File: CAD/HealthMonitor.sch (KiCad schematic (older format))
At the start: 8 parts

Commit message: Created sheet hierarchy"
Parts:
- removed C1: 1u, symbol Device:C
- removed D1, D2: LED_green, symbol Device:LED
- removed D3: LED_ir, symbol Device:LED
- removed R1, R2, R3: 10k, symbol Device:R
- removed U?: BH1792GLC, symbol bh1792glc:BH1792GLC
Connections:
- net labels removed: GND, VCC
- wire segments 33 -> 0
- no-connect marks 1 -> 0
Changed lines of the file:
@@
 EESchema Schematic File Version 4
+LIBS:HealthMonitor-cache
 EELAYER 26 0
 EELAYER END
 $Descr A4 11693 8268
 encoding utf-8
-Sheet 1 1
+Sheet 1 2
 Title ""
 Date ""
@@
 Comment4 ""
 $EndDescr
-$Comp
-L bh1792glc:BH1792GLC U?
-U 1 1 5CC0C673
-P 6050 3400
-F 0 "U?" H 6025 3865 50  0000 C CNN
-F 1 "BH1792GLC" H 6025 3774 50  0000 C CNN
-F 2 "" H 6050 3400 50  0001 C CNN
-F 3 "" H 6050 3400 50  0001 C CNN
-	1    6050 3400
-	1    0    0    -1
-$EndComp
-$Comp
-L Device:LED D3
-U 1 1 5CC0C7AE
-P 4500 2950
-F 0 "D3" V 4550 3250 50  0000 R CNN
-F 1 "LED_ir" V 4450 3300 50  0000 R CNN
-F 2 "" H 4500 2950 50  0001 C CNN
-F 3 "~" H 4500 2950 50  0001 C CNN
-	1    4500 2950
-	0    -1   -1   0
-$EndComp
-Wire Wire Line
-	5500 3400 5000 3400
-Wire Wire Line
-	5000 3400 5000 3100
-Wire Wire Line
-	4750 3500 4750 3100
-Wire Wire Line
-	4750 3500 5500 3500
-Wire Wire Line
-	4500 3600 5500 3600
-$Comp
-L Device:LED D2
-U 1 1 5CC0C8EA
-P 4750 2950
-F 0 "D2" V 4800 2850 50  0000 R CNN
-F 1 "LED_green" V 4900 3100 50  0000 R CNN
-F 2 "" H 4750 2950 50  0001 C CNN
-F 3 "~" H 4750 2950 50  0001 C CNN
-	1    4750 2950
-	0    -1   -1   0
-$EndComp
-$Comp
-L Device:LED D1
-U 1 1 5CC0C908
-P 5000 2950
-F 0 "D1" V 5038 2832 50  0000 R CNN
-F 1 "LED_green" V 4950 2850 50  0000 R CNN
-F 2 "" H 5000 2950 50  0001 C CNN
-F 3 "~" H 5000 2950 50  0001 C CNN
-	1    5000 2950
-	0    -1   -1   0
-$EndComp
-Wire Wire Line
-	4500 3100 4500 3600
-Wire Wire Line
-	4500 2800 4500 2600
-Wire Wire Line
-	4500 2600 4750 2600
-Wire Wire Line
-	5000 2600 5000 2800
-Wire Wire Line
-	4750 2800 4750 2600
-Connection ~ 4750 2600
-Wire Wire Line
-	5500 3200 5500 2600
-Wire Wire Line
-	5500 2600 5400 2600
-Connection ~ 5000 2600
-$Comp
-L power:GND #PWR?
-U 1 1 5CC0CC3B
-P 5350 3300
-F 0 "#PWR?" H 5350 3050 50  0001 C CNN
-F 1 "GND" V 5355 3172 50  0000 R CNN
-F 2 "" H 5350 3300 50  0001 C CNN
-F 3 "" H 5350 3300 50  0001 C CNN
-	1    5350 3300
-	0    1    1    0
-$EndComp
-Wire Wire Line
-	5350 3300 5400 3300
-$Comp
-L power:VCC #PWR?
-U 1 1 5CC0CDAD
-P 5050 2500
-F 0 "#PWR?" H 5050 2350 50  0001 C CNN
-F 1 "VCC" H 5067 2673 50  0000 C CNN
-F 2 "" H 5050 2500 50  0001 C CNN
-F 3 "" H 5050 2500 50  0001 C CNN
-	1    5050 2500
-	1    0    0    -1
-$EndComp
-Wire Wire Line
-	5050 2500 5050 2600
-Connection ~ 5050 2600
-Wire Wire Line
-	5050 2600 5000 2600
-Wire Wire Line
-	4750 2600 5000 2600
-$Comp
-L Device:C C1
-U 1 1 5CC0D0E2
-P 5400 2900
-F 0 "C1" H 5515 2946 50  0000 L CNN
-F 1 "1u" H 5515 2855 50  0000 L CNN
-F 2 "" H 5438 2750 50  0001 C CNN
-F 3 "~" H 5400 2900 50  0001 C CNN
-	1    5400 2900
-	1    0    0    -1
-$EndComp
-Connection ~ 5400 3300
-Wire Wire Line
-	5400 3300 5500 3300
-Connection ~ 5400 2600
-Wire Wire Line
-	5400 2600 5050 2600
-Wire Wire Line
-	5400 2750 5400 2600
-Wire Wire Line
-	5400 3050 5400 3300
-$Comp
-L Device:R R1
-U 1 1 5CC0D78E
-P 6700 2850
-F 0 "R1" H 6770 2896 50  0000 L CNN
-F 1 "10k" H 6770 2805 50  0000 L CNN
-F 2 "" V 6630 2850 50  0001 C CNN
-F 3 "~" H 6700 2850 50  0001 C CNN
-	1    6700 2850
-	1    0    0    -1
-$EndComp
-$Comp
-L Device:R R2
-U 1 1 5CC0D826
-P 6950 2850
-F 0 "R2" H 7020 2896 50  0000 L CNN
-F 1 "10k" H 7020 2805 50  0000 L CNN
-F 2 "" V 6880 2850 50  0001 C CNN
-F 3 "~" H 6950 2850 50  0001 C CNN
-	1    6950 2850
-	1    0    0    -1
-$EndComp
-$Comp
-L Device:R R3
-U 1 1 5CC0D850
-P 7200 2850
-F 0 "R3" H 7270 2896 50  0000 L CNN
-F 1 "10k" H 7270 2805 50  0000 L CNN
-F 2 "" V 7130 2850 50  0001 C CNN
-F 3 "~" H 7200 2850 50  0001 C CNN
-	1    7200 2850
-	1    0    0    -1
-$EndComp
-Wire Wire Line
-	7200 2700 7200 2600
-Wire Wire Line
-	7200 2600 6950 2600
-Connection ~ 5500 2600
-Wire Wire Line
-	6700 2700 6700 2600
-Connection ~ 6700 2600
-Wire Wire Line
-	6700 2600 5500 2600
-Wire Wire Line
-	6950 2700 6950 2600
-Connection ~ 6950 2600
-Wire Wire Line
-	6950 2600 6700 2600
-Wire Wire Line
-	6700 3000 6700 3200
-Wire Wire Line
-	6700 3200 6550 3200
-Wire Wire Line
-	6550 3300 6950 3300
-Wire Wire Line
-	6950 3300 6950 3000
-Wire Wire Line
-	6550 3600 7200 3600
-Wire Wire Line
-	7200 3600 7200 3000
-$Comp
-L power:GND #PWR?
-U 1 1 5CC0E6E1
-P 6700 3500
-F 0 "#PWR?" H 6700 3250 50  0001 C CNN
-F 1 "GND" V 6705 3372 50  0000 R CNN
-F 2 "" H 6700 3500 50  0001 C CNN
-F 3 "" H 6700 3500 50  0001 C CNN
-	1    6700 3500
-	0    -1   -1   0
-$EndComp
-Wire Wire Line
-	6550 3500 6700 3500
-NoConn ~ 6550 3400
+$Sheet
+S 8050 2800 1600 2300
+U 5CD03BDA
+F0 "bh1792-interface" 50
+F1 "bh1792-interface.sch" 50
+$EndSheet
 $EndSCHEMATC

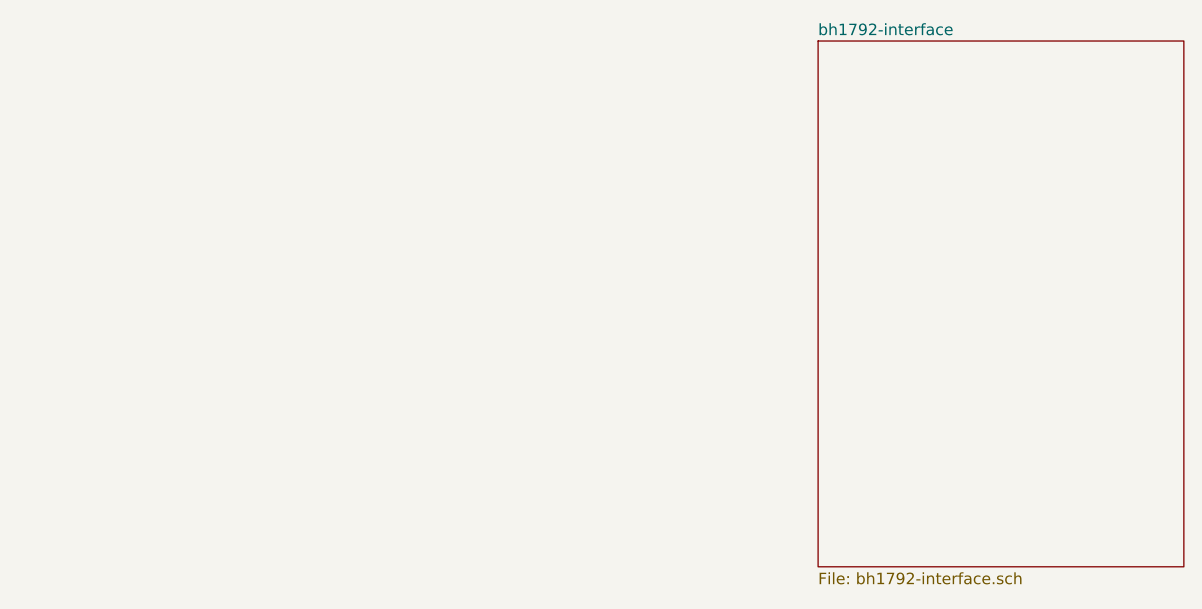
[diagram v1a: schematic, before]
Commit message: Created Power PCB, both schematic and layout
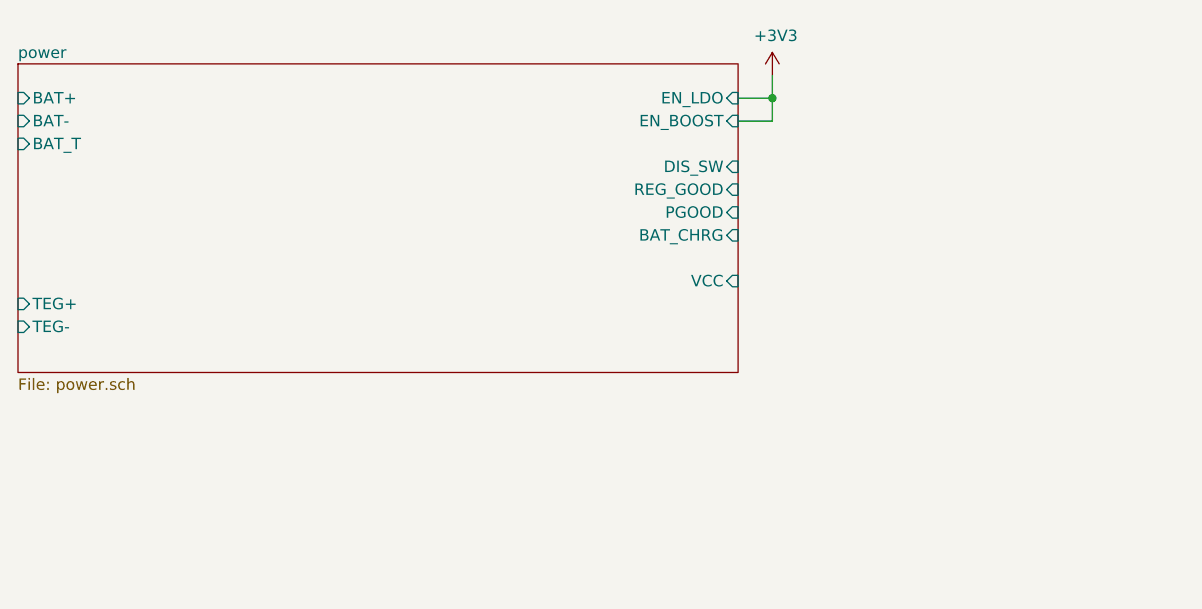
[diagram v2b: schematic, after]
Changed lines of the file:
@@
 $EndDescr
 $Sheet
-S 8050 2800 1600 2300
-U 5CD03BDA
-F0 "bh1792-interface" 50
-F1 "bh1792-interface.sch" 50
+S 4550 2900 3150 1350
+U 5CD0623C
+F0 "power" 50
+F1 "power.sch" 50
+F2 "BAT+" I L 4550 3050 50
+F3 "EN_LDO" I R 7700 3050 50
+F4 "EN_BOOST" I R 7700 3150 50
+F5 "DIS_SW" I R 7700 3350 50
+F6 "REG_GOOD" I R 7700 3450 50
+F7 "PGOOD" I R 7700 3550 50
+F8 "BAT-" I L 4550 3150 50
+F9 "TEG+" I L 4550 3950 50
+F10 "TEG-" I L 4550 4050 50
+F11 "BAT_T" I L 4550 3250 50
+F12 "BAT_CHRG" I R 7700 3650 50
+F13 "VCC" I R 7700 3850 50
 $EndSheet
+Wire Wire Line
+	7700 3150 7850 3150
+Wire Wire Line
+	7850 3050 7700 3050
+Wire Wire Line
+	7850 3050 7850 3150
+$Comp
+L power:+3V3 #PWR0101
+U 1 1 5CD4D077
+P 7850 2950
+F 0 "#PWR0101" H 7850 2800 50  0001 C CNN
+F 1 "+3V3" H 7865 3123 50  0000 C CNN
+F 2 "" H 7850 2950 50  0001 C CNN
+F 3 "" H 7850 2950 50  0001 C CNN
+	1    7850 2950
+	1    0    0    -1
+$EndComp
+Wire Wire Line
+	7850 2950 7850 3050
+Connection ~ 7850 3050
 $EndSCHEMATC

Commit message: Finished PCB Draft -- waiting for review
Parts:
- added J1: BAT_T, Connector_PinHeader_1.27mm:PinHeader_1x01_P1.27mm_Vertical, symbol Connector:Conn_01x01_Male
- added J10, J20: SDA, Connector_PinHeader_1.27mm:PinHeader_1x01_P1.27mm_Vertical, symbol Connector:Conn_01x01_Male
- added J11, J21: SCL, Connector_PinHeader_1.27mm:PinHeader_1x01_P1.27mm_Vertical, symbol Connector:Conn_01x01_Male
- added J12, J25: DIS_SW, Connector_PinHeader_1.27mm:PinHeader_1x01_P1.27mm_Vertical, symbol Connector:Conn_01x01_Male
- added J13, J24: BAT_CHRG, Connector_PinHeader_1.27mm:PinHeader_1x01_P1.27mm_Vertical, symbol Connector:Conn_01x01_Male
- added J14: USBDP, Connector_PinHeader_1.27mm:PinHeader_1x01_P1.27mm_Vertical, symbol Connector:Conn_01x01_Male
- added J15: USBDM, Connector_PinHeader_1.27mm:PinHeader_1x01_P1.27mm_Vertical, symbol Connector:Conn_01x01_Male
- added J16: USB_V, Connector_PinHeader_1.27mm:PinHeader_1x01_P1.27mm_Vertical, symbol Connector:Conn_01x01_Male
- added J17: VBUS, Connector_PinHeader_1.27mm:PinHeader_1x01_P1.27mm_Vertical, symbol Connector:Conn_01x01_Male
- added J18: D+, Connector_PinHeader_1.27mm:PinHeader_1x01_P1.27mm_Vertical, symbol Connector:Conn_01x01_Male
- added J19: D-, Connector_PinHeader_1.27mm:PinHeader_1x01_P1.27mm_Vertical, symbol Connector:Conn_01x01_Male
- added J2: TEG+, Connector_PinHeader_1.27mm:PinHeader_1x01_P1.27mm_Vertical, symbol Connector:Conn_01x01_Male
- added J22, J8: VCC, Connector_PinHeader_1.27mm:PinHeader_1x01_P1.27mm_Vertical, symbol Connector:Conn_01x01_Male
- added J23, J9: GND, Connector_PinHeader_1.27mm:PinHeader_1x01_P1.27mm_Vertical, symbol Connector:Conn_01x01_Male
- added J3: TEG-, Connector_PinHeader_1.27mm:PinHeader_1x01_P1.27mm_Vertical, symbol Connector:Conn_01x01_Male
- added J4: BAT-, Connector_PinHeader_1.27mm:PinHeader_1x01_P1.27mm_Vertical, symbol Connector:Conn_01x01_Male
- added J5: BAT+, Connector_PinHeader_1.27mm:PinHeader_1x01_P1.27mm_Vertical, symbol Connector:Conn_01x01_Male
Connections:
- net +3V3: now also J22.1 (Pin_1), J8.1 (Pin_1)
- net power/BAT+: now also J5.1 (Pin_1)
- net power/BAT_T: now also J1.1 (Pin_1)
- net power/TEG+: now also J2.1 (Pin_1)
- new net BAT_CHRG: J13.1 (Pin_1), J24.1 (Pin_1)
- new net DIS_SW: J12.1 (Pin_1), J25.1 (Pin_1)
- new net GND: J23.1 (Pin_1), J3.1 (Pin_1), J4.1 (Pin_1), J9.1 (Pin_1)
- new net SCL: J11.1 (Pin_1), J21.1 (Pin_1)
- new net SDA: J10.1 (Pin_1), J20.1 (Pin_1)
- new net power/USBD+: J14.1 (Pin_1), J18.1 (Pin_1)
- new net power/USBD-: J15.1 (Pin_1), J19.1 (Pin_1)
- new net power/USB_VBUS: J16.1 (Pin_1), J17.1 (Pin_1)

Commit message: rescue commit
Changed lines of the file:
@@
-$EndSheet
-$Sheet
-S 8750 950  1350 2000
-U 5CD82074
-F0 "IMUSensor" 50
-F1 "IMUSensor.sch" 50
-F2 "VDD" I L 8750 1150 50
-F3 "SCL" I L 8750 1450 50
-F4 "SDA-SDISDO" B L 8750 1550 50
-F5 "SDO-SA0" B L 8750 1650 50
-F6 "CS" I L 8750 1750 50
-F7 "INT2" O L 8750 2000 50
-F8 "INT1" O L 8750 2100 50
-F9 "GND" U L 8750 1250 50
 $EndSheet
 $Sheet
@@
 Wire Wire Line
 	8200 3550 8900 3550
+$Sheet
+S 8750 950  1350 2000
+U 5CD82074
+F0 "IMUSensor" 50
+F1 "IMUSensor.sch" 50
+F2 "VDD" I L 8750 1150 50
+F3 "SCL" I L 8750 1450 50
+F4 "INT2" O L 8750 2000 50
+F5 "INT1" O L 8750 2100 50
+F6 "GND" U L 8750 1250 50
+F7 "SDA" B L 8750 1550 50
+$EndSheet
 $EndSCHEMATC
